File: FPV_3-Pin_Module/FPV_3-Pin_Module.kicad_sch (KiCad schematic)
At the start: 3 parts, among them J2 Conn_01x03_Socket, J2 Conn_01x10_Socket, J3 Conn_01x10_Socket

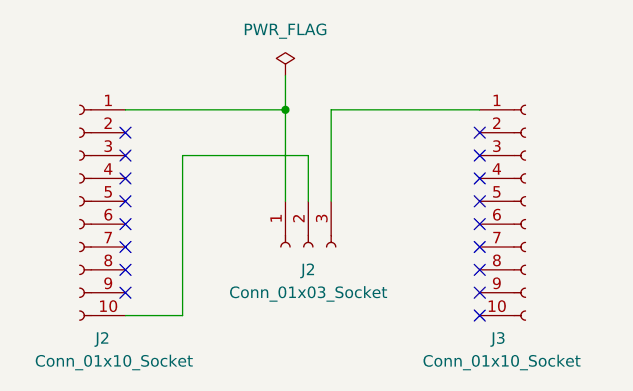
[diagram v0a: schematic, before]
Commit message: Adding FPV 4-pin interface module
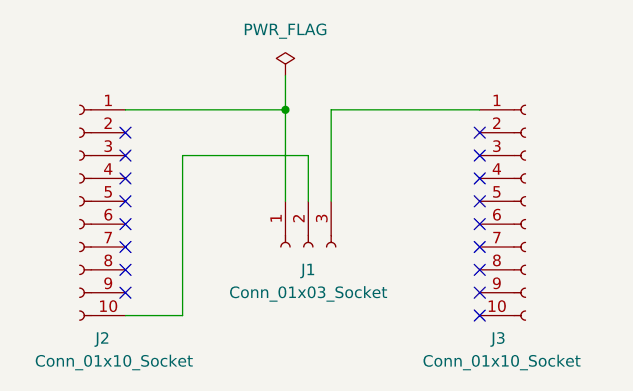
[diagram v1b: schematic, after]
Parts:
- renumbered J2 to J1
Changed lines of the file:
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@@
   (symbol (lib_id "Connector:Conn_01x03_Socket") (at 142.24 93.98 90) (mirror x) (unit 1)
     (in_bom yes) (on_board yes) (dnp no)
-    (property "Reference" "J2" (at 142.24 96.52 90)
+    (property "Reference" "J1" (at 142.24 96.52 90)
       (effects (font (size 1.27 1.27)))
     )
@@
       (project "FPV_3-Pin_Module"
         (path "/d88b4443-d914-4b47-8a50-2a5201342e50"
-          (reference "J2") (unit 1)
+          (reference "J1") (unit 1)
         )
       )
@@
       (project "FPV_3-Pin_Module"
         (path "/d88b4443-d914-4b47-8a50-2a5201342e50"
-          (reference "J1") (unit 1)
+          (reference "J2") (unit 1)
         )
       )
